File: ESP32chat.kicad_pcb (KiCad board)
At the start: 2 copper layers, 117.5 x 99.1 mm, 112 parts, among them J1 CONN_021X02_NO_SILK, J2 CONN_021X02_NO_SILK, J3 CONN_01, Q1 Si1308, Q2 BSS123, U1 tp4056_KoreanHropartsElecTYPE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, U2 RFM69HCW, U3 ESP32, U4 BUZZER, U5 FPCConn, U6 RT9013, U7 MCP73831T-2ACI/OT, X1 uFL

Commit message: DRAFT Still needs silk screen, would be nice to remove errors.
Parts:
- moved R11 90.8 mm to (189.2, 67.2), turned to -90 degrees
- moved C20 89.4 mm to (189.2, 71.0), turned to -90 degrees
- moved U6 84.5 mm to (186.1, 67.4), turned to 180 degrees
- moved C19 83.2 mm to (186.1, 70.6), turned to 180 degrees
- moved C21 77.8 mm to (182.9, 67.4), turned to 90 degrees
- moved C22 73.5 mm to (181.0, 67.5), turned to 90 degrees
- moved R5 1.66 mm to (95.1, 73.4), turned to -90 degrees
- moved U13 1.27 mm to (197.5, 99.1)
- moved J1 1.14 mm to (137.8, 59.2)
- moved R4 0.83 mm to (93.5, 73.2), turned to 90 degrees
- moved R6 0.18 mm to (93.5, 76.1), turned to -90 degrees
- moved R1 0.18 mm to (88.9, 65.5)
- moved R2 0.13 mm to (88.9, 63.6)
- turned C11 to 180 degrees
- turned U12 to 0 degrees
- renumbered U$3 to U10, U$5 to U11, U$4 to U12, U$6 to U13, U$7 to U14, U$8 to U15, U$1 to U8, U$2 to U9
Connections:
- net /ROW1 renamed /IO15
- U3 pad 10: /COL08 -> /COL02
- U3 pad 11: /COL09 -> /COL03
- U3 pad 12: /RXLED -> /COL04
- U3 pad 15: /COL11 -> /COL05
- U3 pad 16: /LORA_SCK -> /COL06
- U3 pad 17: /ROW03 -> /COL07
- U3 pad 18: /ROW04 -> /COL08
- U3 pad 19: /COL04 -> /COL09
- U3 pad 20: /COL05 -> /COL10
- U3 pad 21: /COL06 -> /COL11
- U3 pad 22: /COL07 -> /ROW01
- U3 pad 23: /LORA_MOSI -> /ROW02
- U3 pad 24: /LORA_IRQ -> /ROW03
- U3 pad 25: /LORA_RST -> /ROW04
- U3 pad 26: /LORA_MISO -> /EPD_MOSI
- U3 pad 28: /EPD_BUSY -> /EPD_CLK
- U3 pad 29: /EPD_RST -> /EPD_CS
- U3 pad 31: /SPEAKPWM -> /EPD_RST
- U3 pad 32: /EPD_CS -> /EPD_BUSY
- U3 pad 33: /EPD_CLK -> /SPEAKPWM
- U3 pad 34: /EPD_MISO -> /LORA_MISO
- U3 pad 35: /EPD_MOSI -> /LORA_MOSI
- U3 pad 36: /IO44 -> /LORA_SCK
- U3 pad 37: /IO43 -> /LORA_CS
- U3 pad 38: /COL10 -> /LORA_RST
- U3 pad 39: /COL10 -> /LORA_IRQ
- U3 pad 4: /COL02 -> /TXLED
- U3 pad 5: /ROW02 -> /RXLED
- U3 pad 6: /COL01 -> /IO06
- U3 pad 7: /COL03 -> /IO07
- U3 pad 9: /TXLED -> /COL01
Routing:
- net /ROW03: track 0.00 -> 237.0 mm, vias 0 -> 4
- net /COL11: track 0.00 -> 189.5 mm, vias 0 -> 4
- net /ROW04: track 0.00 -> 177.4 mm
- net /ROW02: track 0.00 -> 167.2 mm
- net /ROW01: track 0.00 -> 141.9 mm
- net /COL10: track 0.00 -> 133.9 mm
- net /COL09: track 0.00 -> 125.4 mm
- net /COL08: track 0.00 -> 115.9 mm
- net /COL07: track 0.00 -> 110.4 mm
- net /COL06: track 0.00 -> 95.8 mm
- net /EPD_MOSI: track 0.00 -> 94.2 mm
- net /EPD_CLK: track 0.00 -> 91.9 mm
- net /EPD_CS: track 0.00 -> 90.9 mm
- net /COL05: track 0.00 -> 90.0 mm
- net /EPD_DC: track 0.00 -> 89.9 mm
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- added copper zone on In1.Cu, net +3.3V
- added copper zone on B.Cu, net GND
- added copper zone on F.Cu, net GND
- added copper zone on In2.Cu, net GND
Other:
- copper layers 2 -> 4

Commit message: Almost ready for review.
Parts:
- moved U1 0.72 mm to (87.8, 73.2)
- moved R5 0.66 mm to (94.5, 73.4)
- moved R3 0.66 mm to (92.8, 70.1)
- moved R4 0.66 mm to (92.8, 73.2)
- moved R6 0.66 mm to (92.9, 76.1)
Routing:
- net /COL10: track 133.9 -> 132.6 mm
- net /EPD_VCOM: track 8.33 -> 9.22 mm
- net /D-: track 4.77 -> 5.43 mm
- net /D+: track 6.53 -> 7.19 mm
- net /COL08: track 115.9 -> 115.4 mm
- net VBAT: vias 2 -> 6
- net GND: vias 215 -> 225
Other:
- board text added: "1 2 3 4 5 6 7 8 9 0 BSP"
- board text added: "A S D F G H J K L ^"
- board text added: "ENTER"
- board text added: "ESP32 LORA Chat"
- board text added: "Q W E R T Y U I O P"
- board text added: "R0.1"
- board text added: "SPACE"
- board text added: "Z X C V B N M . < V >"

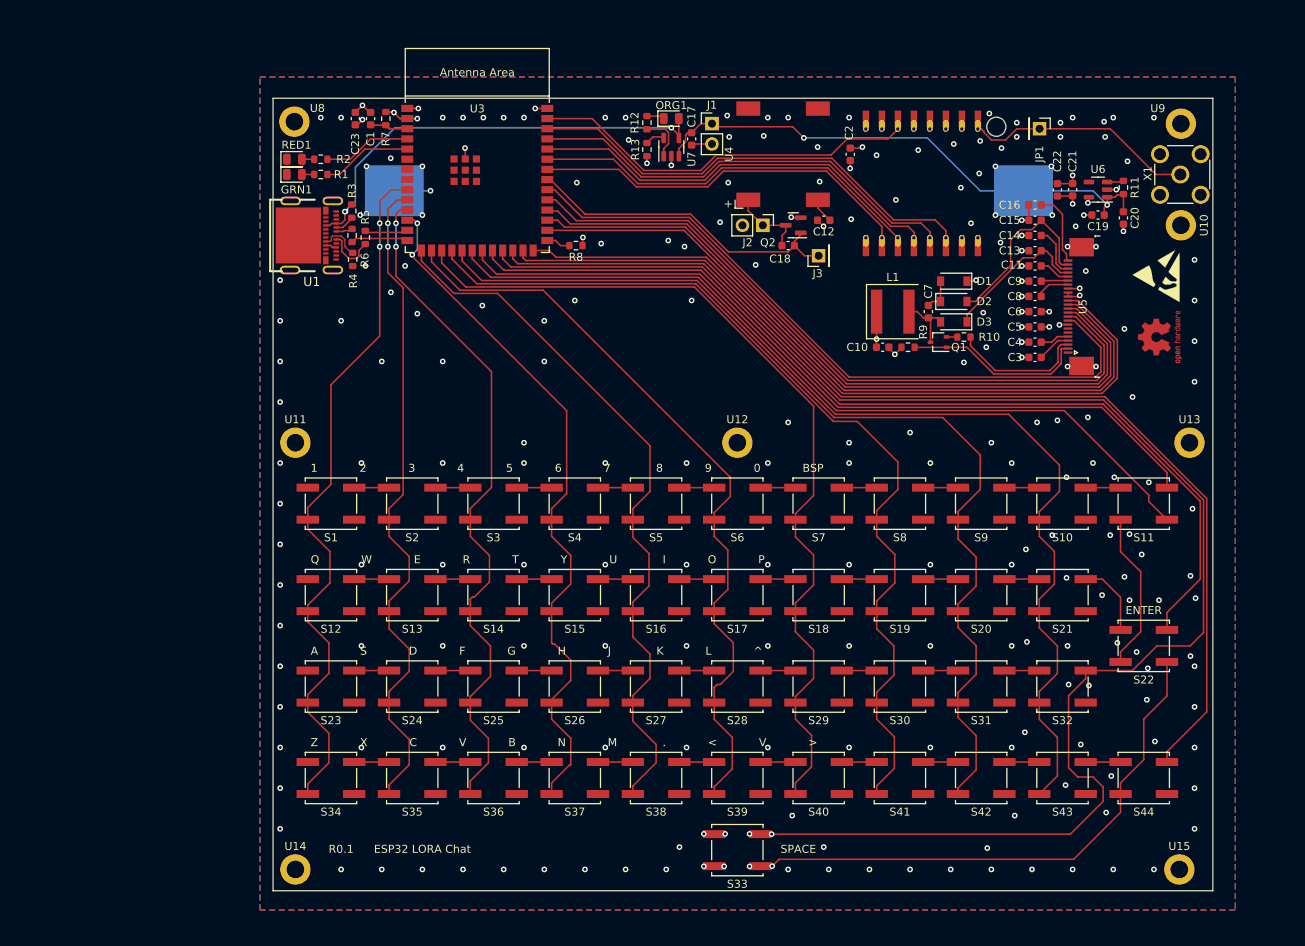
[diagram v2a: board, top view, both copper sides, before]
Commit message: DRAFT laying down copper now, many traces still need to be installed. Checked in for archival purposes.
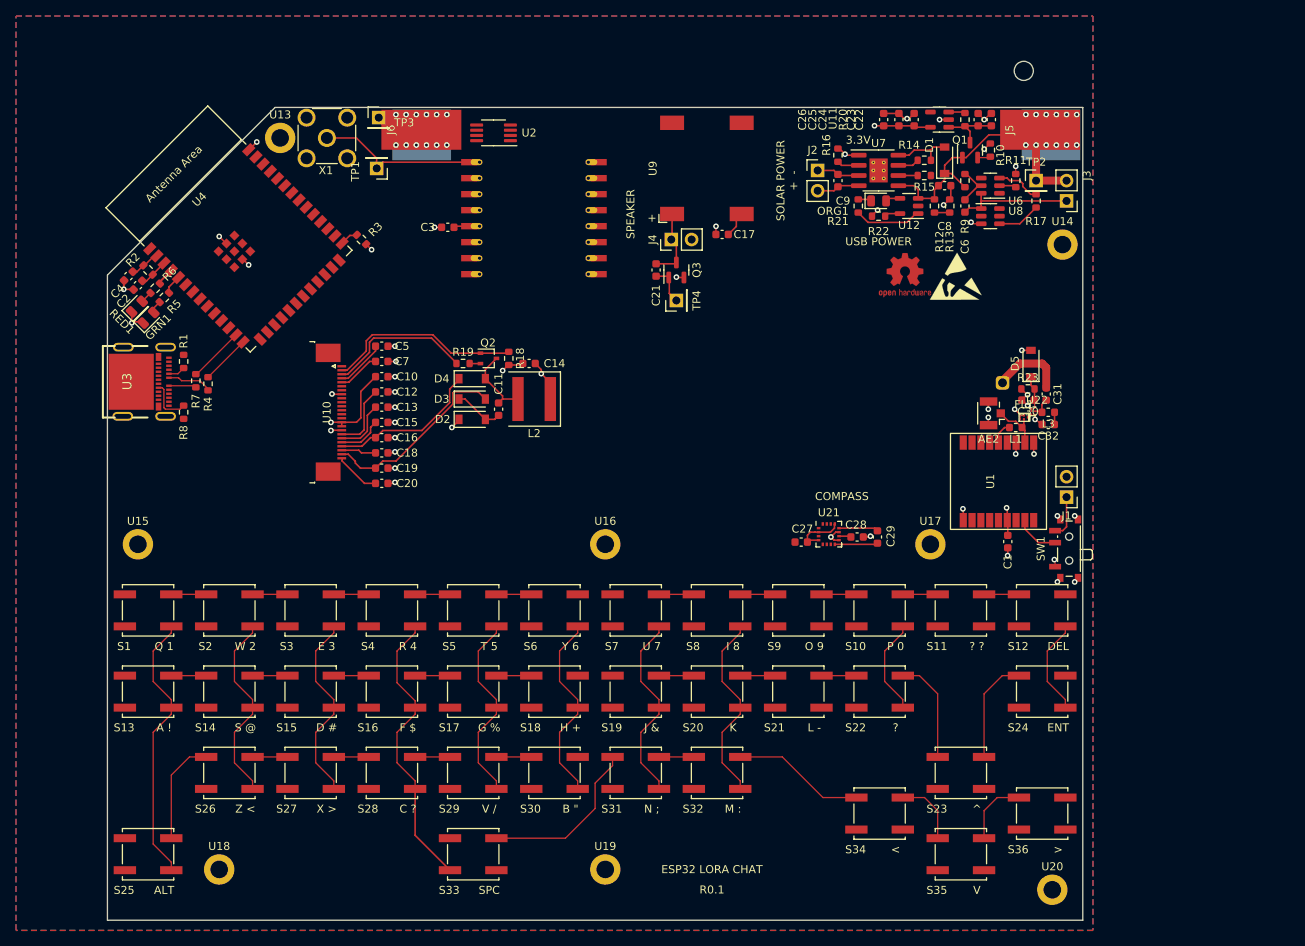
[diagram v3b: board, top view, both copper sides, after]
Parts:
- removed JP1: CONN_01, Connector_PinHeader_2.54mm:PinHeader_1x01_P2.54mm_Vertical
- removed S37, S43: V, KICAD_Footprints:TS-1187A-C-G-B
- removed S38: B, KICAD_Footprints:TS-1187A-C-G-B
- removed S39: N, KICAD_Footprints:TS-1187A-C-G-B
- removed S40: M, KICAD_Footprints:TS-1187A-C-G-B
- removed S41: ., KICAD_Footprints:TS-1187A-C-G-B
- removed S42: <, KICAD_Footprints:TS-1187A-C-G-B
- removed S44: >, KICAD_Footprints:TS-1187A-C-G-B
- added AE1: Antenna, KICAD_Footprints:KH-GPS181804-WY, B.Cu at (174.1, 91.6)
- added AE2: Conn_Coaxial, Connector_Coaxial:U.FL_Hirose_U.FL-R-SMT-1_Vertical, F.Cu at (172.8, 95.4)
- added C24: 10u, Capacitor_SMD:C_0603_1608Metric, F.Cu at (163.1, 58.7)
- added C25: 10u, Capacitor_SMD:C_0603_1608Metric, F.Cu at (161.2, 58.7)
- added C26: 1u, Capacitor_SMD:C_0603_1608Metric, F.Cu at (159.3, 58.7)
- added C27: 1u, Capacitor_SMD:C_0603_1608Metric, F.Cu at (149.0, 111.5)
- added C28: 4.7uF, Capacitor_SMD:C_0603_1608Metric, F.Cu at (155.9, 110.8)
- added C29: 220n, Capacitor_SMD:C_0603_1608Metric, F.Cu at (158.5, 110.8)
- added C30: 1n, Capacitor_SMD:C_0603_1608Metric, F.Cu at (177.3, 93.7)
- added C31: 1.2p, Capacitor_SMD:C_0603_1608Metric, F.Cu at (179.6, 93.0)
- added C32: 6.8p, Capacitor_SMD:C_0603_1608Metric, F.Cu at (179.8, 96.8)
- added D4: MBR0530, Diode_SMD:D_SOD-123, F.Cu at (107.8, 91.1)
- added D5: MBR0530, Diode_SMD:D_SOD-123, F.Cu at (177.7, 89.2)
- added FL1: TA1661A, KICAD_Footprints:TA1661A, F.Cu at (176.8, 95.9)
- added J4: CONN_021X02_NO_SILK, Connector_PinHeader_2.54mm:PinHeader_1x02_P2.54mm_Vertical, F.Cu at (132.7, 73.7)
- added J5: CONN_01, Connector_Wire:SolderWirePad_1x01_SMD_5x10mm, F.Cu at (178.8, 59.9)
- added J6: CONN_01, Connector_Wire:SolderWirePad_1x01_SMD_5x10mm, F.Cu at (101.5, 59.9)
- added L2: 68uh, Inductor_SMD:L_Coilcraft_XAL60xx_6.36x6.56mm, F.Cu at (115.6, 93.6)
- added L3: 6.2nH, Inductor_SMD:L_0603_1608Metric, F.Cu at (179.8, 95.3)
- added Q3: BSS123, Package_TO_SOT_SMD:SOT-23, F.Cu at (133.3, 77.5)
- added R14: 10K, Resistor_SMD:R_0603_1608Metric, F.Cu at (164.3, 63.8)
- added R15: 10K, Resistor_SMD:R_0603_1608Metric, F.Cu at (164.3, 65.7)
- added R16: 10K, Resistor_SMD:R_0603_1608Metric, F.Cu at (153.5, 63.1)
- added R17: 0R, Resistor_SMD:R_0603_1608Metric, F.Cu at (178.3, 68.8)
- added R18: 10K, Resistor_SMD:R_0603_1608Metric, F.Cu at (112.4, 88.5)
- added R19: 0R47, Resistor_SMD:R_0603_1608Metric, F.Cu at (106.7, 89.2)
- added R20: 10K, Resistor_SMD:R_0603_1608Metric, F.Cu at (169.4, 58.7)
- added R21: 1K, Resistor_SMD:R_0603_1608Metric, F.Cu at (156.1, 69.5)
- added R22: 5K1, Resistor_SMD:R_0603_1608Metric, F.Cu at (158.6, 70.7)
- added R23: 10K, Resistor_SMD:R_0603_1608Metric, F.Cu at (177.3, 92.3)
- added SW1: SW_DIP_x01, Button_Switch_SMD:SW_SPDT_PCM12, F.Cu at (182.1, 112.3)
- added TP1: CONN_01, Connector_PinHeader_2.54mm:PinHeader_1x01_P2.54mm_Vertical, F.Cu at (95.9, 64.8)
- added TP2: CONN_01, Connector_PinHeader_2.54mm:PinHeader_1x01_P2.54mm_Vertical, F.Cu at (178.3, 66.3)
- added TP3: CONN_01, Connector_PinHeader_2.54mm:PinHeader_1x01_P2.54mm_Vertical, F.Cu at (96.1, 58.4)
- added TP4: CONN_01, Connector_PinHeader_2.54mm:PinHeader_1x01_P2.54mm_Vertical, F.Cu at (133.3, 81.3)
- added U16: MOUNTINGHOLE2.0, MountingHole:MountingHole_2.2mm_M2_DIN965_Pad, F.Cu at (124.5, 111.8)
- added U17: MOUNTINGHOLE2.0, MountingHole:MountingHole_2.2mm_M2_DIN965_Pad, F.Cu at (165.1, 111.8)
- added U18: MOUNTINGHOLE2.0, MountingHole:MountingHole_2.2mm_M2_DIN965_Pad, F.Cu at (76.2, 152.4)
- added U19: MOUNTINGHOLE2.0, MountingHole:MountingHole_2.2mm_M2_DIN965_Pad, F.Cu at (124.5, 152.4)
- added U20: MOUNTINGHOLE2.0, MountingHole:MountingHole_2.2mm_M2_DIN965_Pad, F.Cu at (180.3, 154.9)
- added U21: QMC5883L, Package_LGA:LGA-16_3x3mm_P0.5mm, F.Cu at (152.4, 110.5)
- added U22: BGU8019, KICAD_Footprints:XSON6, F.Cu at (177.9, 95.1)
- C1: value 1U -> 10u
- C10, C9: value 1u -> 100n
- C11: value 1u -> 4.7uF
- C12: value 10u -> 1u
- C17, C22: value 10µF -> 10u
- C18: value 100n -> 1u
- C19: value 10µF -> 1u
- C2: value 10uF -> 1u
- C20, C23: value 1µF -> 1u
- C21: value 10µF -> 100n
- C3, C8: value 1u -> 10u
- C5: value 1U -> 1u
- C7: value 4.7uF -> 1u
- J3: value CONN_01 -> CONN_021X02_NO_SILK; footprint Connector_PinHeader_2.54mm:PinHeader_1x01_P2.54mm_Vertical -> Connector_PinHeader_2.54mm:PinHeader_1x02_P2.54mm_Vertical
- L1: value 68uh -> 6.8nH; footprint Inductor_SMD:L_Coilcraft_XAL60xx_6.36x6.56mm -> Inductor_SMD:L_0603_1608Metric
- Q1: value Si1308 -> Q_PMOS_DGS; footprint Package_TO_SOT_SMD:SOT-323_SC-70 -> Package_TO_SOT_SMD:SOT-23
- Q2: value BSS123 -> Si1308; footprint Package_TO_SOT_SMD:SOT-23 -> Package_TO_SOT_SMD:SOT-323_SC-70
- R1: value 1K5 -> 5K1
- R10: value 0R47 -> 10K
- R11, R8: value 10K -> 1K
- R12: value 1K -> 50K
- R13: value 10K -> 50K
- R2: value 1K5 -> 10K
- R3: value 5.1K -> 10K
- R5: value 0R -> 1K5
- R6: value 1K -> 1K5
- R7: value 10K -> 0R
- R9: value 10K -> 100
- S1: value 1 -> PB22
- S10: value 0 -> PB22
- S11: value BSP -> PB22
- S12: value Q -> PB22
- S13: value W -> PB22
- S14: value E -> PB22
- S15: value R -> PB22
- S16: value T -> PB22
- S17: value Y -> PB22
- S18: value U -> PB22
- S19: value I -> PB22
- S2: value 2 -> PB22
- S20: value O -> PB22
- S21: value P -> PB22
- S22: value ENT -> PB22
- S23: value A -> PB22
- S24: value S -> PB22
- S25: value D -> PB22
- S26: value F -> PB22
- S27: value G -> PB22
- S28: value H -> PB22
- S29: value J -> PB22
- S3: value 3 -> PB22
- S30: value K -> PB22
- S31: value L -> PB22
- S32: value ^ -> PB22
- S33: value _ -> PB22
- S34: value Z -> PB22
- S35: value X -> PB22
- S36: value C -> PB22
- S4: value 4 -> PB22
- S5: value 5 -> PB22
- S6: value 6 -> PB22
- S7: value 7 -> PB22
- S8: value 8 -> PB22
- S9: value 9 -> PB22
- U1: value tp4056_KoreanHropartsElecTYPE-C-31-M-12 -> ATGM336H-5N31; footprint KICAD_Footprints:USB-C_SMD-TYPE-C-31-M-12 -> KICAD_Footprints:ATGM336H-5N
- U10: value MOUNTINGHOLE2.0 -> FPCConn; footprint MountingHole:MountingHole_2.2mm_M2_DIN965_Pad -> KICAD_Footprints:TE_2-1734839-4_1x24-1MP_P0.5mm_Horizontal_2
- U11: value MOUNTINGHOLE2.0 -> RT9013; footprint MountingHole:MountingHole_2.2mm_M2_DIN965_Pad -> Package_TO_SOT_SMD:SOT-23-5
- U12: value MOUNTINGHOLE2.0 -> MCP73831T-2ACI/OT; footprint MountingHole:MountingHole_2.2mm_M2_DIN965_Pad -> Package_TO_SOT_SMD:SOT-23-5
- U2: value RFM69HCW -> LM75B; footprint KICAD_Footprints:RFM69HCW -> Package_SO:MSOP-8_3x3mm_P0.65mm
- U3: value ESP32 -> tp4056_KoreanHropartsElecTYPE-C-31-M-12; footprint KICAD_Footprints:ESP32-S3-WROOM-1 -> KICAD_Footprints:USB-C_SMD-TYPE-C-31-M-12
- U4: value BUZZER -> ESP32; footprint KICAD_Footprints:FS-1340 -> KICAD_Footprints:ESP32-S3-WROOM-1
- U5: value FPCConn -> RFM69HCW; footprint KICAD_Footprints:TE_2-1734839-4_1x24-1MP_P0.5mm_Horizontal_2 -> KICAD_Footprints:RFM69HCW
- U6: value RT9013 -> DW01; footprint Package_TO_SOT_SMD:SOT-23-5 -> Package_TO_SOT_SMD:SOT-23-6
- U7: value MCP73831T-2ACI/OT -> TP4056; footprint Package_TO_SOT_SMD:SOT-23-5 -> Package_SO:SOIC-8-1EP_3.9x4.9mm_P1.27mm_EP2.29x3mm_ThermalVias
- U8: value MOUNTINGHOLE2.0 -> FS8205A; footprint MountingHole:MountingHole_2.2mm_M2_DIN965_Pad -> Package_TO_SOT_SMD:SOT-23-6
- U9: value MOUNTINGHOLE2.0 -> BUZZER; footprint MountingHole:MountingHole_2.2mm_M2_DIN965_Pad -> KICAD_Footprints:FS-1340
- moved U15 136.4 mm to (66.0, 111.8)
- moved U14 123.7 mm to (181.6, 74.3)
- moved U13 119.9 mm to (83.8, 61.0)
- moved C4 113.6 mm to (64.9, 78.2), turned to 45 degrees
- moved U10 108.8 mm to (90.2, 95.2)
- moved X1 106.8 mm to (89.7, 61.0), turned to 0 degrees
- moved C20 98.5 mm to (96.5, 104.1), turned to 0 degrees
- moved C1 95.6 mm to (174.8, 111.4)
- moved C19 95.0 mm to (96.5, 102.2), turned to 0 degrees
- moved U1 91.1 mm to (173.6, 103.9)
- moved C2 90.5 mm to (66.0, 79.4), turned to 45 degrees
- moved U11 90.1 mm to (166.2, 58.7), turned to 180 degrees
- moved S12 88.9 mm to (179.1, 120.0)
- moved U8 87.8 mm to (172.6, 70.7)
- moved C16 86.7 mm to (96.5, 98.4), turned to 0 degrees
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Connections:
- BT1 pad 1: VBAT -> +BATT
- BT1 pad 2: GND -> /BAT-
- C1 pad 1: GND -> +3.3V
- C1 pad 2: /EN -> GND
- C10 pad 1: GND -> +3.3V
- C10 pad 2: +3.3V -> GND
- C11 pad 1: /EPD_VSH -> Net-(C11-Pad1)
- C11 pad 2: GND -> Net-(C11-Pad2)
- C12 pad 1: Net-(C12-Pad1) -> /EPD_VDD
- C12 pad 2: +3.3V -> GND
- C13 pad 1: /EPD_PREVGH -> /EPD_VPP
- C14 pad 1: /EPD_VSL -> GND
- C14 pad 2: GND -> +3.3V
- C15 pad 1: /EPD_PREVGL -> /EPD_VSH
- C16 pad 1: /EPD_VCOM -> /EPD_PREVGH
- C17 pad 1: VBAT -> Net-(C17-Pad1)
- C17 pad 2: GND -> +3.3V
- C18 pad 1: /LIN -> /EPD_VSL
- C18 pad 2: /SPEAKPWM -> GND
- C19 pad 1: VBAT -> /EPD_PREVGL
- C2 pad 1: +3.3V -> GND
- C2 pad 2: GND -> /EN
- C20 pad 1: VBAT -> /EPD_VCOM
- C21 pad 1: +3.3V -> /LIN
- C21 pad 2: GND -> /SPEAKPWM
- C22 pad 1: +3.3V -> Vdrive
- C23 pad 1: +3.3V -> Vdrive
- C3 pad 1: /EPD_VGL -> +3.3V
- C4 pad 1: /EPD_VGH -> GND
- C4 pad 2: GND -> +3.3V
- C5 pad 1: GND -> /EPD_VGL
- C5 pad 2: +3.3V -> GND
- C6 pad 1: +3.3V -> Net-(C6-Pad1)
- C6 pad 2: GND -> /BAT-
- C7 pad 1: Net-(C7-Pad1) -> /EPD_VGH
- C7 pad 2: Net-(C7-Pad2) -> GND
- C8 pad 1: /EPD_VDD -> +BATT
- C9 pad 1: /EPD_VPP -> Net-(C9-Pad1)
- D1 pad 1: GND -> +BATT
- D1 pad 2: Net-(C7-Pad2) -> Net-(C9-Pad1)
- D2 pad 1: Net-(C7-Pad2) -> GND
- D2 pad 2: /EPD_PREVGL -> Net-(C11-Pad2)
- D3 pad 1: /EPD_PREVGH -> Net-(C11-Pad2)
- D3 pad 2: Net-(C7-Pad1) -> /EPD_PREVGL
- J1 pad 1: VBAT -> Net-(J1-Pad1)
- J2 pad 1: /LIN -> GND
- J2 pad 2: +3.3V -> Net-(C9-Pad1)
- J3 pad 1: /SPEAKPWM -> /BAT-
- L1 pad 1: +3.3V -> /RF_OUT
- L1 pad 2: Net-(C7-Pad1) -> Net-(L1-Pad2)
- Q1 pad 1: /EPD_GDR -> +BATT
- Q1 pad 3: Net-(C7-Pad1) -> Vdrive
- Q2 pad 1: /SPEAKPWM -> /EPD_GDR
- Q2 pad 2: GND -> Net-(Q2-Pad2)
- Q2 pad 3: /LIN -> Net-(C11-Pad1)
- R1 pad 1: /RXLED -> GND
- R1 pad 2: Net-(GRN1-Pad2) -> Net-(R1-Pad2)
- R10 pad 1: /EPD_RESE -> GND
- R11 pad 1: Net-(R11-Pad1) -> GND
- R11 pad 2: VBAT -> Net-(R11-Pad2)
- R12 pad 1: Net-(ORG1-Pad1) -> +BATT
- R12 pad 2: Net-(R12-Pad2) -> /VBATadc
- R13 pad 1: GND -> /VBATadc
- R13 pad 2: Net-(R13-Pad2) -> GND
- R2 pad 1: /TXLED -> +3.3V
- R2 pad 2: Net-(R2-Pad2) -> /EN
- R3 pad 1: GND -> +3.3V
- R5 pad 1: /D- -> /RXLED
- R5 pad 2: /DN -> Net-(GRN1-Pad2)
- R6 pad 1: Net-(R6-Pad1) -> /TXLED
- R6 pad 2: GND -> Net-(R6-Pad2)
- R7 pad 1: +3.3V -> /D-
- R7 pad 2: /EN -> /DN
- R8 pad 1: +3.3V -> Net-(R8-Pad1)
- R8 pad 2: Net-(R8-Pad2) -> GND
- R9 pad 1: /EPD_GDR -> +BATT
- R9 pad 2: GND -> Net-(C6-Pad1)
- RED1 pad 2: Net-(R2-Pad2) -> Net-(R6-Pad2)
- S10 pad 1: /ROW01 -> /ROW04
- S10 pad 2: /COL10 -> /COL03
- S11 pad 1: /ROW01 -> /ROW04
- S11 pad 2: /COL11 -> /COL02
- S12 pad 1: /ROW02 -> /ROW04
- S13 pad 2: /COL02 -> /COL01
- S14 pad 2: /COL03 -> /COL02
- S15 pad 2: /COL04 -> /COL03
- S16 pad 2: /COL05 -> /COL04
- S17 pad 2: /COL06 -> /COL05
- S18 pad 2: /COL07 -> /COL06
- S19 pad 1: /ROW02 -> /ROW05
- S19 pad 2: /COL08 -> /COL06
- S20 pad 1: /ROW02 -> /ROW05
- S20 pad 2: /COL09 -> /COL05
- S21 pad 1: /ROW02 -> /ROW05
- S21 pad 2: /COL10 -> /COL04
- S22 pad 1: /ROW02 -> /ROW05
- S22 pad 2: /COL11 -> /COL03
- S23 pad 1: /ROW03 -> /ROW05
- S23 pad 2: /COL01 -> /COL02
- S24 pad 1: /ROW03 -> /ROW05
- S24 pad 2: /COL02 -> /COL01
- S25 pad 2: /COL03 -> /COL01
- S26 pad 2: /COL04 -> /COL02
- S27 pad 2: /COL05 -> /COL03
- S28 pad 2: /COL06 -> /COL04
- S29 pad 2: /COL07 -> /COL05
- S30 pad 2: /COL08 -> /COL06
- S31 pad 1: /ROW03 -> /ROW06
- S31 pad 2: /COL09 -> /COL06
- S32 pad 1: /ROW03 -> /ROW06
- S32 pad 2: /COL10 -> /COL05
- S33 pad 1: /ROW03 -> /ROW06
- S33 pad 2: /COL11 -> /COL04
- S34 pad 1: /ROW04 -> /ROW06
- S34 pad 2: /COL01 -> /COL03
- S35 pad 1: /ROW04 -> /ROW06
- S36 pad 1: /ROW04 -> /ROW06
- S36 pad 2: /COL03 -> /COL01
- S7 pad 1: /ROW01 -> /ROW04
- S7 pad 2: /COL07 -> /COL06
- S8 pad 1: /ROW01 -> /ROW04
- S8 pad 2: /COL08 -> /COL05
- S9 pad 1: /ROW01 -> /ROW04
- S9 pad 2: /COL09 -> /COL04
- U10 pad 1: unconnected-(U10-Pad1) -> /EPD_HLT_CTL
- U11 pad 1: unconnected-(U11-Pad1) -> Vdrive
- U12 pad 1: unconnected-(U12-Pad1) -> Net-(R21-Pad2)
- U2 pad 1: Net-(JP1-Pad1) -> /I2S_SDA
- U2 pad 2: GND -> /I2S_SCL
- U2 pad 3: /DIO3 -> unconnected-(U2-Pad3)
- U2 pad 4: /DIO4 -> GND
- U2 pad 5: +3.3V -> GND
- U2 pad 6: /LORA_IRQ -> GND
- U2 pad 7: /DIO1 -> GND
- U2 pad 8: /DIO2 -> +3.3V
- U4 pad 1: /LIN -> GND
- U4 pad 2: Net-(C12-Pad1) -> +3.3V
- U4 pad 3: (no net) -> /EN
- U4 pad 4: (no net) -> /TXLED
- U5 pad 1: /EPD_HLT_CTL -> Net-(TP1-Pad1)
- U5 pad 10: /EPD_RST -> /LORA_MISO
- U5 pad 11: /EPD_DC -> /LORA_MOSI
- U5 pad 12: /EPD_CS -> /LORA_SCK
- U5 pad 13: /EPD_CLK -> /LORA_CS
- U5 pad 14: /EPD_MOSI -> /LORA_RST
- U5 pad 15: +3.3V -> /DIO5
- U5 pad 16: +3.3V -> GND
- U5 pad 2: /EPD_GDR -> GND
- U5 pad 3: /EPD_RESE -> /DIO3
- U5 pad 4: /EPD_VGL -> /DIO4
- U5 pad 5: /EPD_VGH -> +3.3V
- U5 pad 6: /EPD_TSCL -> /LORA_IRQ
- U5 pad 7: /EPD_TSDA -> /DIO1
- U5 pad 8: GND -> /DIO2
- U5 pad 9: /EPD_BUSY -> GND
- U6 pad 1: VBAT -> /G1
- U6 pad 2: GND -> Net-(R11-Pad2)
- U6 pad 3: Net-(R11-Pad1) -> /OC
- U6 pad 5: +3.3V -> Net-(C6-Pad1)
- U7 pad 1: Net-(R12-Pad2) -> GND
- U7 pad 2: GND -> /PROG
- U7 pad 3: VBAT -> GND
- U7 pad 4: VBUS -> Net-(C9-Pad1)
- U7 pad 5: Net-(R13-Pad2) -> +BATT
- U8 pad 1: unconnected-(U8-Pad1) -> /BAT-
- U9 pad 1: unconnected-(U9-Pad1) -> /LIN
- X1 pad 1: Net-(JP1-Pad1) -> Net-(TP1-Pad1)
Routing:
- net /ROW03: track 237.0 -> 30.6 mm, vias 4 -> 0
- net /COL11: track 189.5 -> 0.00 mm, vias 4 -> 0
- net /ROW04: track 177.4 -> 21.8 mm
- net /ROW02: track 167.2 -> 21.8 mm
- net /COL10: track 132.6 -> 0.00 mm
- net /COL09: track 125.3 -> 0.00 mm
- net /ROW01: track 141.9 -> 21.8 mm
- net /COL08: track 115.4 -> 0.00 mm
- net /COL07: track 110.3 -> 0.00 mm
- net /EPD_MOSI: track 94.2 -> 0.00 mm
- net /EPD_CLK: track 91.9 -> 0.00 mm
- net /EPD_CS: track 90.9 -> 0.00 mm
- net /EPD_DC: track 89.9 -> 0.00 mm
- net /EPD_RST: track 88.8 -> 0.00 mm
- net /EPD_BUSY: track 87.7 -> 0.00 mm
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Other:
- board size 117.5 x 99.1 mm -> 121.9 x 101.6 mm
- board text added: "3.3V"
- board text added: "COMPASS"
- board text added: "ESP32 LORA CHAT"
- board text added: "SOLAR POWER + -"
- board text added: "SPEAKER"
- board text added: "USB POWER"
- board text removed: "1 2 3 4 5 6 7 8 9 0 BSP"
- board text removed: "A S D F G H J K L ^"
- board text removed: "ENTER"
- board text removed: "ESP32 LORA Chat"
- board text removed: "Q W E R T Y U I O P"
- board text removed: "SPACE"
- board text removed: "Z X C V B N M . < V >"

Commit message: DRAFT Almost ready for review again. Checking in for archival purposes.
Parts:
- added TP10: CONN_01, KICAD_Footprints:TST_x01_P2.54mm_Vertical, B.Cu at (96.9, 80.3)
- added TP11: CONN_01, KICAD_Footprints:TST_x01_P2.54mm_Vertical, B.Cu at (91.6, 81.4)
- added TP12: CONN_01, KICAD_Footprints:TST_x01_P2.54mm_Vertical, B.Cu at (90.3, 83.4)
- added TP13: CONN_01, KICAD_Footprints:TST_x01_P2.54mm_Vertical, B.Cu at (89.8, 74.9)
- added TP14: CONN_01, KICAD_Footprints:TST_x01_P2.54mm_Vertical, B.Cu at (87.5, 75.4)
- added TP15: CONN_01, KICAD_Footprints:TST_x01_P2.54mm_Vertical, B.Cu at (84.8, 79.8)
- added TP16: CONN_01, KICAD_Footprints:TST_x01_P2.54mm_Vertical, B.Cu at (87.9, 73.0)
- added TP17: CONN_01, KICAD_Footprints:TST_x01_P2.54mm_Vertical, B.Cu at (84.6, 77.2)
- added TP18: CONN_01, KICAD_Footprints:TST_x01_P2.54mm_Vertical, B.Cu at (85.9, 73.8)
- added TP19: CONN_01, KICAD_Footprints:TST_x01_P2.54mm_Vertical, B.Cu at (87.8, 83.4)
- added TP20: CONN_01, KICAD_Footprints:TST_x01_P2.54mm_Vertical, B.Cu at (92.3, 68.8)
- added TP21: CONN_01, KICAD_Footprints:TST_x01_P2.54mm_Vertical, B.Cu at (90.3, 67.7)
- added TP22: CONN_01, KICAD_Footprints:TST_x01_P2.54mm_Vertical, B.Cu at (99.7, 66.2)
- added TP23: CONN_01, KICAD_Footprints:TST_x01_P2.54mm_Vertical, B.Cu at (99.7, 68.2)
- added TP24: CONN_01, KICAD_Footprints:TST_x01_P2.54mm_Vertical, B.Cu at (80.1, 84.5)
- added TP25: CONN_01, KICAD_Footprints:TST_x01_P2.54mm_Vertical, B.Cu at (71.6, 75.9)
- added TP26: CONN_01, KICAD_Footprints:TST_x01_P2.54mm_Vertical, B.Cu at (74.0, 75.4)
- added TP27: CONN_01, KICAD_Footprints:TST_x01_P2.54mm_Vertical, B.Cu at (73.4, 77.7)
- added TP28: CONN_01, KICAD_Footprints:TST_x01_P2.54mm_Vertical, B.Cu at (75.7, 77.1)
- added TP29: CONN_01, KICAD_Footprints:TST_x01_P2.54mm_Vertical, B.Cu at (78.7, 83.1)
- added TP30: CONN_01, KICAD_Footprints:TST_x01_P2.54mm_Vertical, B.Cu at (81.8, 82.8)
- added TP31: CONN_01, KICAD_Footprints:TST_x01_P2.54mm_Vertical, B.Cu at (81.8, 80.0)
- added TP32: CONN_01, KICAD_Footprints:TST_x01_P2.54mm_Vertical, B.Cu at (83.4, 81.2)
- added TP33: CONN_01, KICAD_Footprints:TST_x01_P2.54mm_Vertical, B.Cu at (75.2, 79.5)
- added TP34: CONN_01, KICAD_Footprints:TST_x01_P2.54mm_Vertical, B.Cu at (77.3, 78.7)
- added TP35: CONN_01, KICAD_Footprints:TST_x01_P2.54mm_Vertical, B.Cu at (77.0, 81.3)
- added TP36: CONN_01, KICAD_Footprints:TST_x01_P2.54mm_Vertical, B.Cu at (78.9, 80.1)
- added TP37: CONN_01, KICAD_Footprints:TST_x01_P2.54mm_Vertical, B.Cu at (80.3, 81.5)
- added TP5: CONN_01, KICAD_Footprints:TST_x01_P2.54mm_Vertical, B.Cu at (77.2, 65.8)
- added TP6: CONN_01, KICAD_Footprints:TST_x01_P2.54mm_Vertical, B.Cu at (80.5, 69.1)
- added TP7: CONN_01, KICAD_Footprints:TST_x01_P2.54mm_Vertical, B.Cu at (78.9, 67.4)
- added TP8: CONN_01, KICAD_Footprints:TST_x01_P2.54mm_Vertical, B.Cu at (82.2, 70.7)
- added TP9: CONN_01, KICAD_Footprints:TST_x01_P2.54mm_Vertical, B.Cu at (89.2, 81.4)
- TP1, TP2, TP3, TP4: footprint Connector_PinHeader_2.54mm:PinHeader_1x01_P2.54mm_Vertical -> KICAD_Footprints:TST_x01_P2.54mm_Vertical; moved to B.Cu
- moved C27 15.3 mm to (142.6, 97.5)
- moved U21 15.3 mm to (146.0, 96.5)
- moved C28 15.3 mm to (149.6, 96.9)
- moved C29 15.2 mm to (152.8, 96.8)
- moved R3 1.53 mm to (95.1, 72.6), turned to 180 degrees
- moved U13 0.92 mm to (83.1, 60.5)
- moved R14 0.51 mm to (163.8, 63.8)
- moved R15 0.51 mm to (163.8, 65.7)
- moved SW1 0.16 mm to (182.1, 112.1)
- moved D5 0.13 mm to (177.7, 89.0)
- moved R23 0.13 mm to (177.3, 92.2)
- moved FL1 0.13 mm to (176.8, 95.8)
- moved R19 0.13 mm to (106.6, 89.2)
- turned TP1 to 0 degrees
- turned TP2 to 180 degrees
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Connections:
- net Net-(R21-Pad2) renamed /USBstat
- U3 pad B4: VBUS -> unconnected-(U3-PadB4)
- U3 pad B6: /DP -> unconnected-(U3-PadB6)
- U3 pad B7: /DN -> unconnected-(U3-PadB7)
- U4 pad 10: /COL02 -> /COL05
- U4 pad 11: /COL03 -> /COL06
- U4 pad 12: /COL04 -> /ROW01
- U4 pad 15: /COL05 -> /ROW02
- U4 pad 16: /COL06 -> /ROW03
- U4 pad 17: unconnected-(U4-Pad17) -> /ROW04
- U4 pad 18: unconnected-(U4-Pad18) -> /ROW05
- U4 pad 19: unconnected-(U4-Pad19) -> /ROW06
- U4 pad 20: unconnected-(U4-Pad20) -> /EPD_MOSI
- U4 pad 21: unconnected-(U4-Pad21) -> /EPD_CLK
- U4 pad 22: /ROW01 -> /EPD_CS
- U4 pad 23: /ROW02 -> /EPD_DC
- U4 pad 24: /ROW03 -> /EPD_RST
- U4 pad 25: /ROW04 -> /EPD_BUSY
- U4 pad 26: /EPD_MOSI -> /COMP_DATA_READY
- U4 pad 28: /EPD_CLK -> /LORA_MISO
- U4 pad 29: /EPD_CS -> /LORA_MOSI
- U4 pad 30: /EPD_DC -> /LORA_SCK
- U4 pad 31: /EPD_RST -> /LORA_CS
- U4 pad 32: /EPD_BUSY -> /LORA_IRQ
- U4 pad 33: /SPEAKPWM -> /LORA_RST
- U4 pad 34: /LORA_MISO -> /I2S_SCL
- U4 pad 35: /LORA_MOSI -> /I2S_SDA
- U4 pad 38: /LORA_RST -> /SPEAKPWM
- U4 pad 39: /LORA_IRQ -> /VBATadc
- U4 pad 6: /IO06 -> /COL01
- U4 pad 7: /IO07 -> /COL02
- U4 pad 8: /IO15 -> /COL03
- U4 pad 9: /COL01 -> /COL04
- U7 pad 9: unconnected-(U7-Pad9) -> Net-(C9-Pad1)
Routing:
- net /COL01: track 46.3 -> 261.2 mm, vias 0 -> 2
- net /COL02: track 24.1 -> 233.3 mm, vias 0 -> 2
- net /COL03: track 36.1 -> 232.2 mm, vias 0 -> 2
- net /COL04: track 36.0 -> 199.4 mm, vias 0 -> 2
- net /ROW06: track 59.2 -> 177.6 mm
- net /GPS_RX: track 0.00 -> 115.4 mm, vias 0 -> 2
- net /ROW04: track 21.8 -> 134.5 mm
- net /GPS_TX: track 0.00 -> 112.4 mm, vias 0 -> 2
- net VBUS: track 1.87 -> 109.5 mm, vias 0 -> 3
- net /COL05: track 48.1 -> 155.2 mm, vias 0 -> 2
- net /VBATadc: track 1.91 -> 106.8 mm, vias 0 -> 3
- net /ROW05: track 39.5 -> 139.6 mm
- net /COL06: track 48.1 -> 148.2 mm, vias 0 -> 2
- net /ROW03: track 30.6 -> 130.1 mm
- net /I2S_SDA: track 0.00 -> 96.3 mm, vias 0 -> 2
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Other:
- rule pad_to_mask_clearance: 0 -> 0.0762

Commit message: Ready for review.
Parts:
- renumbered C2 to C1, C26 to C10, C21 to C11, C17 to C12, C3 to C13, C31 to C14, C14 to C15, C32 to C16, C30 to C17, C11 to C18, C27 to C19, C9 to C2, C7 to C20, C10 to C21, C13 to C22, C16 to C23, C19 to C24, C5 to C25, C12 to C26, C15 to C27, C18 to C28, C20 to C29, C4 to C3, C28 to C30, C29 to C31, C1 to C32, C22 to C4, C8 to C5, C23 to C6, C24 to C7, C6 to C8, C25 to C9, D5 to D2, D2 to D3, D3 to D4, D4 to D5, J2 to J1, J5 to J2, J6 to J3, J3 to J4, J4 to J5, J1 to J6, L3 to L1, L1 to L3, Q3 to Q2, Q2 to Q3, R2 to R1, R17 to R10, R9 to R11, R4 to R13, R7 to R14, R13 to R15, R10 to R16, R1 to R17, R8 to R18, R23 to R19, R3 to R2, R18 to R20, R5 to R21, R6 to R22, R19 to R23, R14 to R3, R15 to R4, R22 to R5, R21 to R6, R16 to R7, R11 to R8, R20 to R9, S4 to S10, S16 to S11, S28 to S12, S5 to S13, S17 to S14, S29 to S15, S6 to S16, S18 to S17, S30 to S18, S7 to S19, S13 to S2, S19 to S20, S31 to S21, S8 to S22, S20 to S23, S32 to S24, S9 to S25, S21 to S26, S33 to S27, S10 to S28, S22 to S29, S25 to S3, S34 to S30, S11 to S31, S23 to S32, S35 to S33, S12 to S34, S24 to S35, S2 to S4, S14 to S5, S26 to S6, S3 to S7, S15 to S8, S27 to S9, TP5 to TP1, TP31 to TP10, TP32 to TP11, TP15 to TP12, TP17 to TP13, TP19 to TP14, TP33 to TP15, TP34 to TP16, TP35 to TP17, TP36 to TP18, TP2 to TP19, TP7 to TP2, TP3 to TP20, TP6 to TP21, TP8 to TP22, TP9 to TP23, TP10 to TP24, TP37 to TP25, TP11 to TP26, TP12 to TP27, TP13 to TP28, TP14 to TP29, TP24 to TP3, TP16 to TP30, TP18 to TP31, TP20 to TP32, TP21 to TP33, TP23 to TP34, TP22 to TP35, TP4 to TP36, TP1 to TP37, TP25 to TP4, TP26 to TP5, TP27 to TP6, TP28 to TP7, TP29 to TP8, TP30 to TP9, U12 to U1, U13 to U10, U17 to U11, U14 to U12, U18 to U13, U15 to U14, U19 to U15, U20 to U17, U22 to U18, U2 to U19, U7 to U2, U1 to U20, U10 to U22, U4 to U3, U8 to U4, U6 to U5, U11 to U6, U5 to U7, U3 to U8
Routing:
- net GND: track 93.6 -> 93.5 mm, vias 311 -> 316
- net /VBATadc: vias 3 -> 2
